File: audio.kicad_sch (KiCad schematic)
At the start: 1 part, among them U7 PCM5122PW

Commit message: External I/O
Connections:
- net AUDIO_L_OUT: now reaches U7.6 (OUTL)
- net AUDIO_R_OUT: now reaches U7.7 (OUTR)
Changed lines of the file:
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@@
+		)
+	)
+	(hierarchical_label "AUDIO_L_OUT"
+		(shape output)
+		(at 165.1 82.55 0)
+		(effects
+			(font
+				(size 1.27 1.27)
+			)
+			(justify left)
+		)
+	)
+	(hierarchical_label "AUDIO_R_OUT"
+		(shape output)
+		(at 165.1 85.09 0)
+		(effects
+			(font
+				(size 1.27 1.27)
+			)
+			(justify left)
 		)
 	)

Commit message: Internal Connectors
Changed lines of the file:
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@@
 	(bus
 		(pts
-			(xy 121.92 80.01) (xy 116.84 80.01)
+			(xy 121.92 80.01) (xy 121.92 77.47)
 		)
 		(stroke
@@
 	(hierarchical_label "{I2S}"
 		(shape input)
-		(at 116.84 80.01 180)
+		(at 121.92 77.47 90)
 		(effects
 			(font
 				(size 1.27 1.27)
 			)
-			(justify right)
+			(justify left)
 		)
 	)

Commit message: Cleanup & Debug I/O
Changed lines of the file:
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@@
+		)
+	)
+	(hierarchical_label "AUD_RST_N"
+		(shape input)
+		(at 120.65 100.33 180)
+		(effects
+			(font
+				(size 1.27 1.27)
+			)
+			(justify right)
 		)
 	)

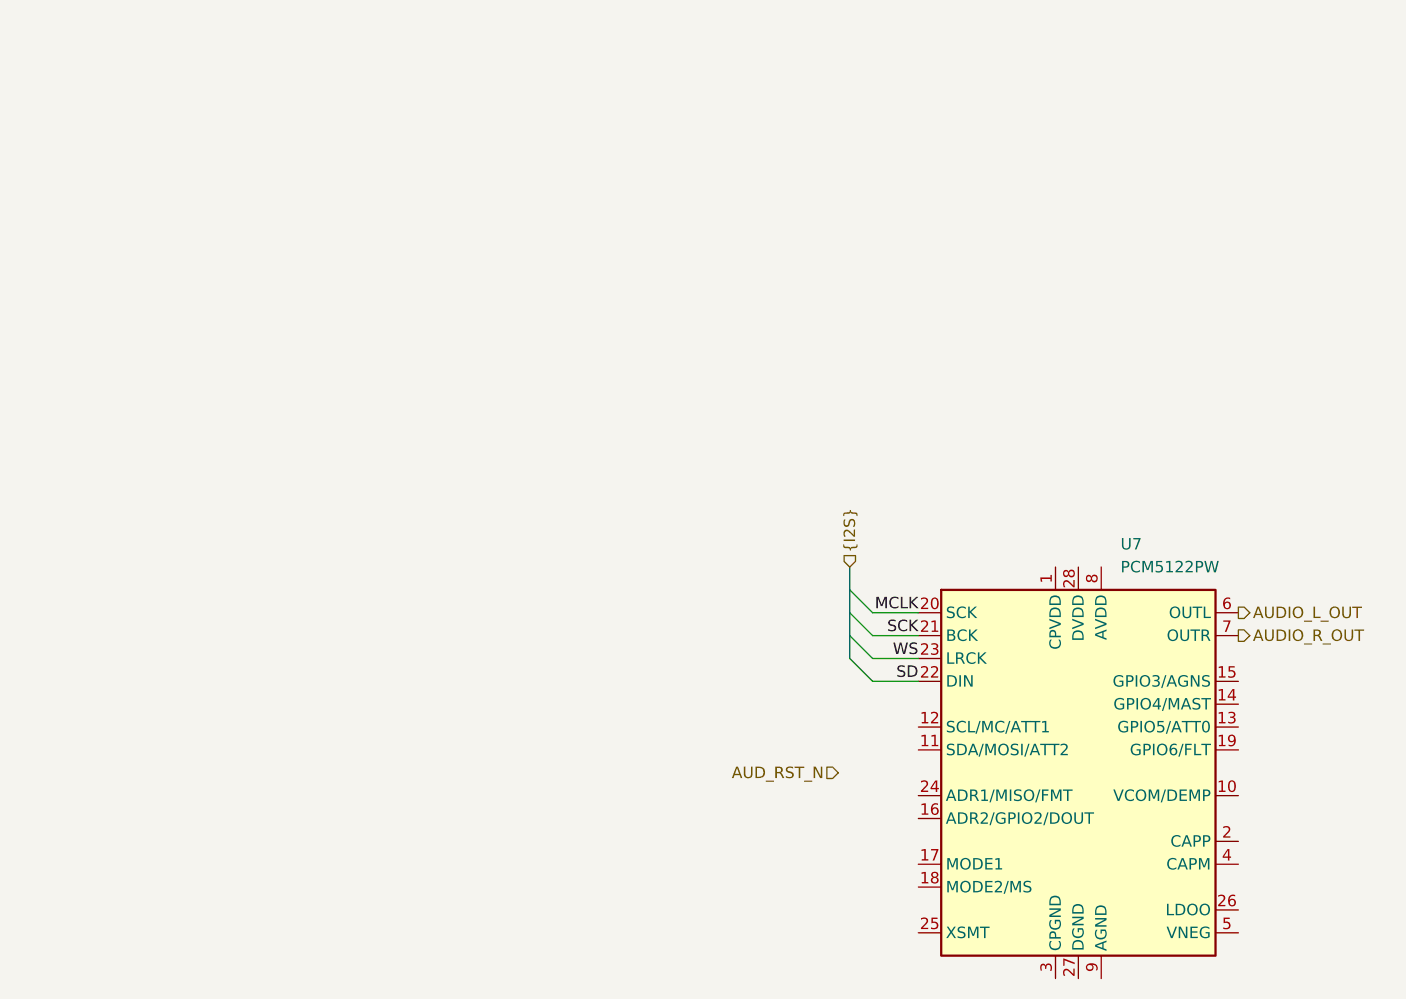
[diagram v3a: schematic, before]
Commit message: Audio Output, Analog isolation and TOSLINK
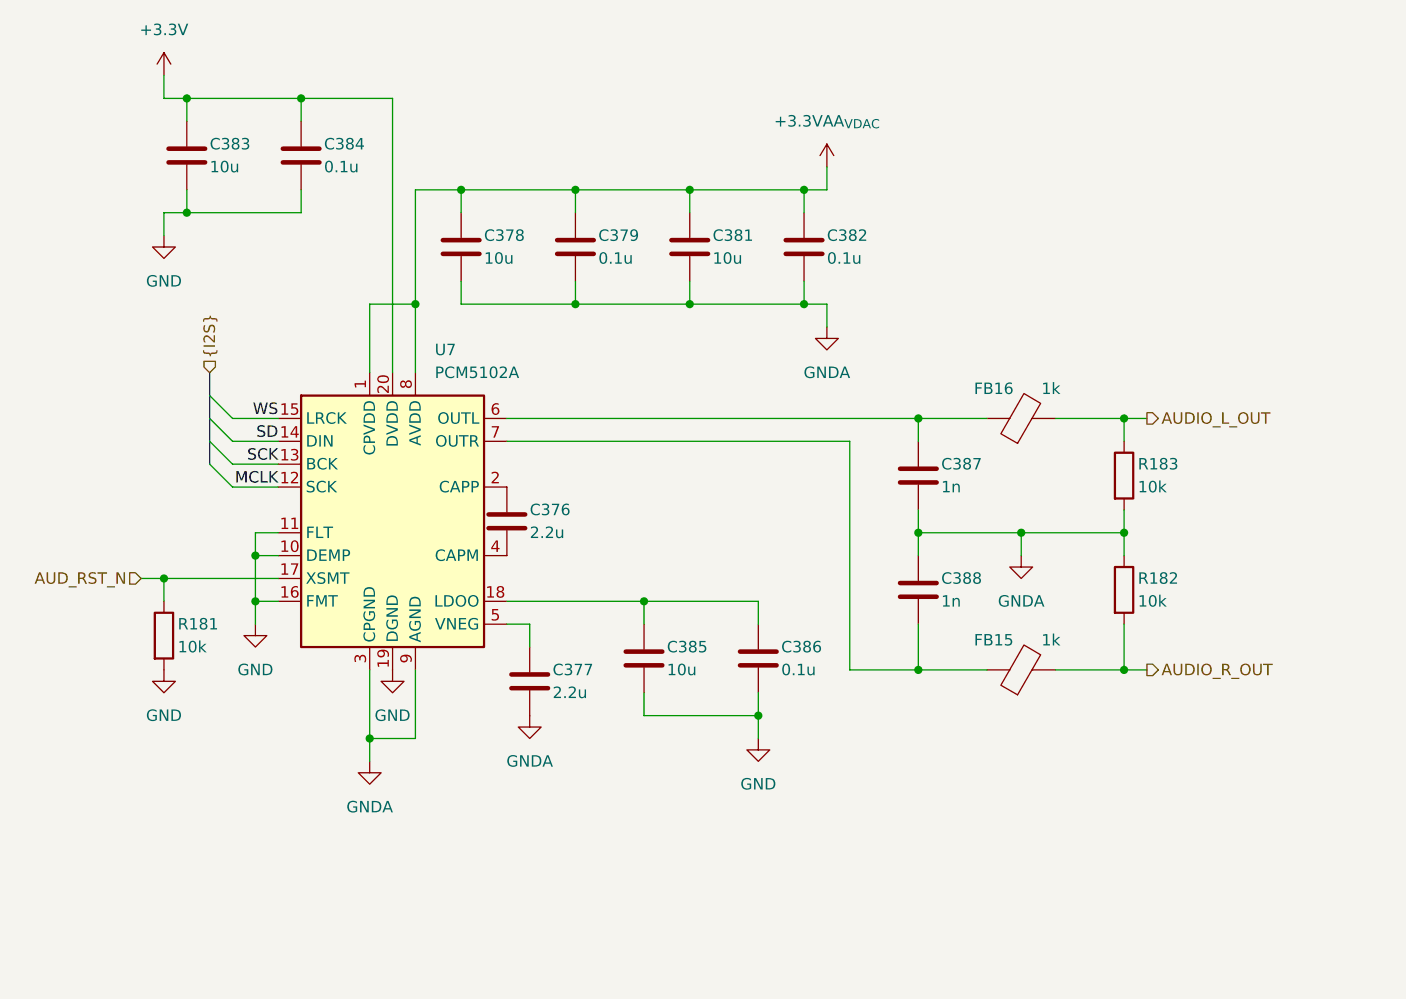
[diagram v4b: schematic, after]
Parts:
- removed U7: PCM5122PW, Package_SO:TSSOP-28_4.4x9.7mm_P0.65mm, symbol Audio:PCM5122PW
- added C376, C377: 2.2u, symbol Device:C
- added C378, C381, C383, C385: 10u, symbol Device:C
- added C379, C382, C384, C386: 0.1u, symbol Device:C
- added C387, C388: 1n, symbol Device:C
- added FB15, FB16: 1k, symbol Device:FerriteBead
- added R181, R182, R183: 10k, symbol Device:R
- added U7: PCM5102A, Package_SO:TSSOP-20_4.4x6.5mm_P0.65mm, symbol Audio:PCM5102A
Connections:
- net AUDIO_L_OUT: now also FB16.2, R183.1
- net AUDIO_R_OUT: now also FB15.2, R182.2
- net AUD_RST_N: now also R181.1, U7.17 (XSMT)
- net MCLK: now also U7.12 (SCK)
- net SCK: now also U7.13 (BCK)
- net SD: now also U7.14 (DIN)
- net WS: now also U7.15 (LRCK)
- new net: C377.1, U7.5 (VNEG)
- new net: C376.1, U7.2 (CAPP)
- new net: C376.2, U7.4 (CAPM)
- new net: C385.1, C386.1, U7.18 (LDOO)
- new net: C387.1, FB16.1, U7.6 (OUTL)
- new net: C388.2, FB15.1, U7.7 (OUTR)
- new net +3.3V: C383.1, C384.1, U7.20 (DVDD)
- new net +3.3VAA_{VDAC}: C378.1, C379.1, C381.1, C382.1, U7.1 (CPVDD), U7.8 (AVDD)
- new net GND: C383.2, C384.2, C385.2, C386.2, R181.2, U7.10 (DEMP), U7.11 (FLT), U7.16 (FMT), U7.19 (DGND)
- new net GNDA: C377.2, C378.2, C379.2, C381.2, C382.2, C387.2, C388.1, R182.1, R183.2, U7.3 (CPGND), U7.9 (AGND)

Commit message: Multipurpose and standby power rails, Reannotated schematic
Added V_1P2, V_1P8, V_5P0DUAL, V_EFUSE, V_GPUPCIE, V_3P3STBY and V_1P2STBY
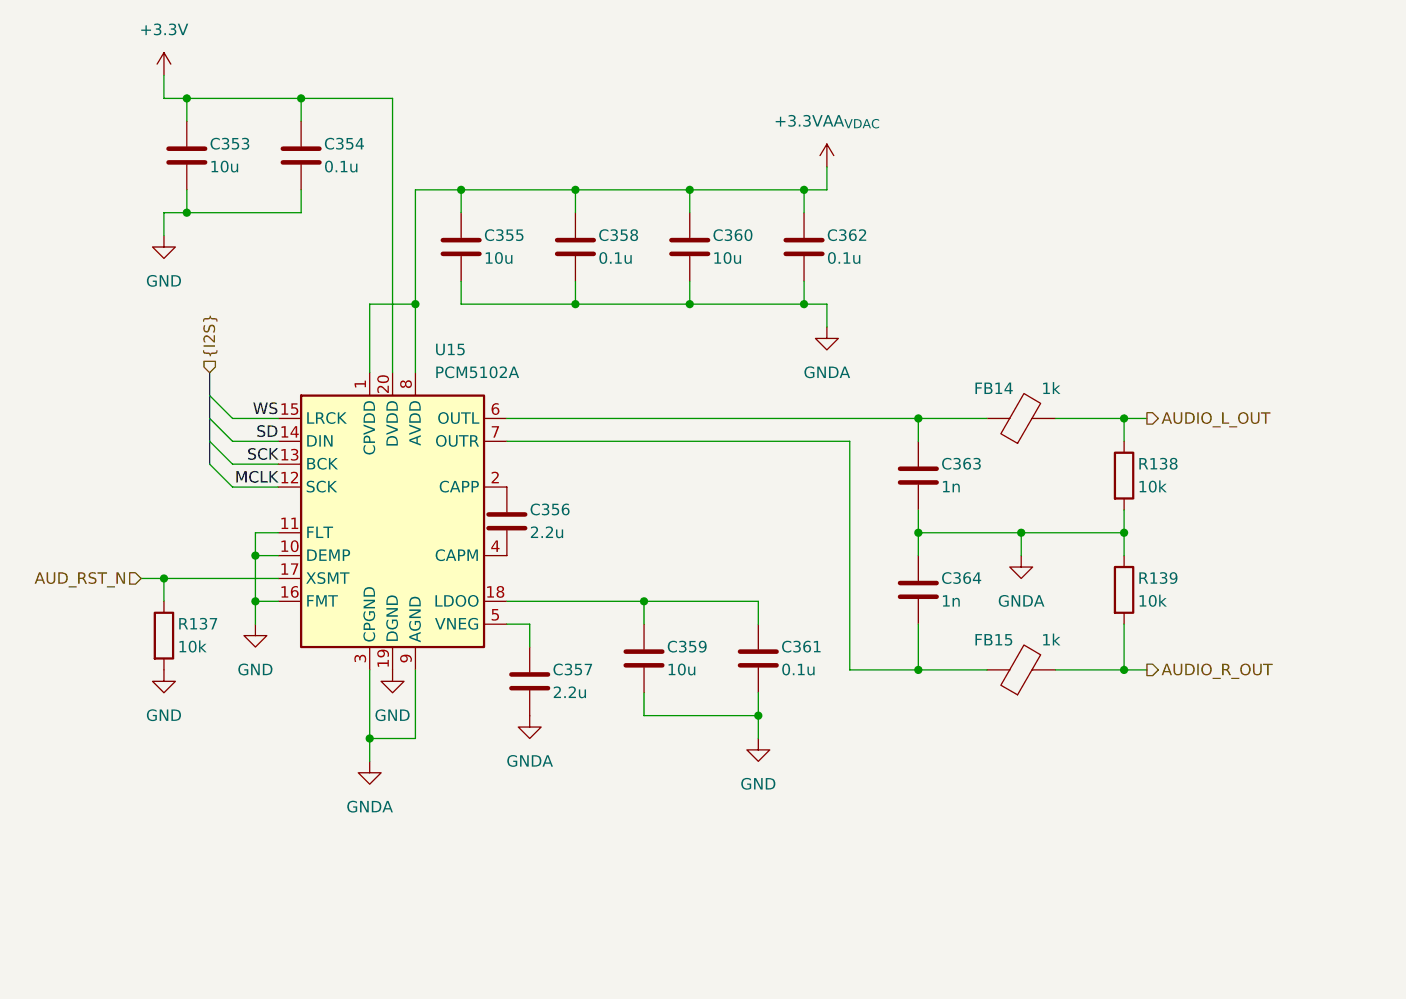
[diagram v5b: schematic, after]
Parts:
- renumbered C383 to C353, C384 to C354, C378 to C355, C376 to C356, C377 to C357, C379 to C358, C385 to C359, C381 to C360, C386 to C361, C382 to C362, C387 to C363, C388 to C364, FB16 to FB14, R181 to R137, R183 to R138, R182 to R139, U7 to U15
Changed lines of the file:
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@@
 		(on_board yes)
 		(dnp no)
-		(property "Reference" "C384"
+		(property "Reference" "C354"
 			(at 63.5 30.48 0)
 			(effects
@@
 			(project "Mantaray"
 				(path "/16640ecb-e4a4-4594-871b-70047bfba6e0/06303de4-2744-44da-b431-31b4ad95c62e"
-					(reference "C384")
+					(reference "C354")
 					(unit 1)
 				)
@@
 		(on_board yes)
 		(dnp no)
-		(property "Reference" "C377"
+		(property "Reference" "C357"
 			(at 88.9 88.9 0)
 			(effects
@@
 			(project "Mantaray"
 				(path "/16640ecb-e4a4-4594-871b-70047bfba6e0/06303de4-2744-44da-b431-31b4ad95c62e"
-					(reference "C377")
+					(reference "C357")
 					(unit 1)
 				)
@@
 		(dnp no)
 		(fields_autoplaced yes)
-		(property "Reference" "#PWR0367"
+		(property "Reference" "#PWR0257"
 			(at 119.38 36.83 0)
 			(effects
@@
 			(project "Mantaray"
 				(path "/16640ecb-e4a4-4594-871b-70047bfba6e0/06303de4-2744-44da-b431-31b4ad95c62e"
-					(reference "#PWR0367")
+					(reference "#PWR0257")
 					(unit 1)
 				)
@@
 		(dnp no)
 		(fields_autoplaced yes)
-		(property "Reference" "#PWR0372"
+		(property "Reference" "#PWR0256"
 			(at 111.76 102.87 0)
 			(effects
@@
 			(project "Mantaray"
 				(path "/16640ecb-e4a4-4594-871b-70047bfba6e0/06303de4-2744-44da-b431-31b4ad95c62e"
-					(reference "#PWR0372")
+					(reference "#PWR0256")
 					(unit 1)
 				)
@@
 		(on_board yes)
 		(dnp no)
-		(property "Reference" "C376"
+		(property "Reference" "C356"
 			(at 86.36 71.12 0)
 			(effects
@@
 			(project "Mantaray"
 				(path "/16640ecb-e4a4-4594-871b-70047bfba6e0/06303de4-2744-44da-b431-31b4ad95c62e"
-					(reference "C376")
+					(reference "C356")
 					(unit 1)
 				)
@@
 		(dnp no)
 		(fields_autoplaced yes)
-		(property "Reference" "#PWR0370"
+		(property "Reference" "#PWR0249"
 			(at 45.72 26.67 0)
 			(effects
@@
 			(project "Mantaray"
 				(path "/16640ecb-e4a4-4594-871b-70047bfba6e0/06303de4-2744-44da-b431-31b4ad95c62e"
-					(reference "#PWR0370")
+					(reference "#PWR0249")
 					(unit 1)
 				)
@@
 		(on_board yes)
 		(dnp no)
-		(property "Reference" "C385"
+		(property "Reference" "C359"
 			(at 101.6 86.36 0)
 			(effects
@@
 			(project "Mantaray"
 				(path "/16640ecb-e4a4-4594-871b-70047bfba6e0/06303de4-2744-44da-b431-31b4ad95c62e"
-					(reference "C385")
+					(reference "C359")
 					(unit 1)
 				)
@@
 		(on_board yes)
 		(dnp no)
-		(property "Reference" "R182"
+		(property "Reference" "R139"
 			(at 153.924 78.74 0)
 			(effects
@@
 			(project "Mantaray"
 				(path "/16640ecb-e4a4-4594-871b-70047bfba6e0/06303de4-2744-44da-b431-31b4ad95c62e"
-					(reference "R182")
+					(reference "R139")
 					(unit 1)
 				)
@@
 		(on_board yes)
 		(dnp no)
-		(property "Reference" "C387"
+		(property "Reference" "C363"
 			(at 132.08 66.04 0)
 			(effects
@@
 			(project "Mantaray"
 				(path "/16640ecb-e4a4-4594-871b-70047bfba6e0/06303de4-2744-44da-b431-31b4ad95c62e"
-					(reference "C387")
+					(reference "C363")
 					(unit 1)
 				)
@@
 		(on_board yes)
 		(dnp no)
-		(property "Reference" "C378"
+		(property "Reference" "C355"
 			(at 81.28 40.64 0)
 			(effects
@@
 			(project "Mantaray"
 				(path "/16640ecb-e4a4-4594-871b-70047bfba6e0/06303de4-2744-44da-b431-31b4ad95c62e"
-					(reference "C378")
+					(reference "C355")
 					(unit 1)
 				)
@@
 		(dnp no)
 		(fields_autoplaced yes)
-		(property "Reference" "#PWR0258"
+		(property "Reference" "#PWR0251"
 			(at 45.72 95.25 0)
 			(effects
@@
 			(project ""
 				(path "/16640ecb-e4a4-4594-871b-70047bfba6e0/06303de4-2744-44da-b431-31b4ad95c62e"
-					(reference "#PWR0258")
+					(reference "#PWR0251")
 					(unit 1)
 				)
@@
 		(dnp no)
 		(fields_autoplaced yes)
-		(property "Reference" "#PWR0371"
+		(property "Reference" "#PWR0254"
 			(at 71.12 95.25 0)
 			(effects
@@
 			(project ""
 				(path "/16640ecb-e4a4-4594-871b-70047bfba6e0/06303de4-2744-44da-b431-31b4ad95c62e"
-					(reference "#PWR0371")
+					(reference "#PWR0254")
 					(unit 1)
 				)
@@
 		(dnp no)
 		(fields_autoplaced yes)
-		(property "Reference" "U7"
+		(property "Reference" "U15"
 			(at 75.8033 53.34 0)
 			(effects
@@
 			(project ""
 				(path "/16640ecb-e4a4-4594-871b-70047bfba6e0/06303de4-2744-44da-b431-31b4ad95c62e"
-					(reference "U7")
+					(reference "U15")
 					(unit 1)
 				)
@@
 		(on_board yes)
 		(dnp no)
-		(property "Reference" "R181"
+		(property "Reference" "R137"
 			(at 47.244 83.82 0)
 			(effects
@@
 			(project "Mantaray"
 				(path "/16640ecb-e4a4-4594-871b-70047bfba6e0/06303de4-2744-44da-b431-31b4ad95c62e"
-					(reference "R181")
+					(reference "R137")
 					(unit 1)
 				)
@@
 		(on_board yes)
 		(dnp no)
-		(property "Reference" "C381"
+		(property "Reference" "C360"
 			(at 106.68 40.64 0)
 			(effects
@@
 			(project "Mantaray"
 				(path "/16640ecb-e4a4-4594-871b-70047bfba6e0/06303de4-2744-44da-b431-31b4ad95c62e"
-					(reference "C381")
+					(reference "C360")
 					(unit 1)
 				)
@@
 		(dnp no)
 		(fields_autoplaced yes)
-		(property "Reference" "#PWR0368"
+		(property "Reference" "#PWR0258"
 			(at 119.38 57.15 0)
 			(effects
@@
 			(project "Mantaray"
 				(path "/16640ecb-e4a4-4594-871b-70047bfba6e0/06303de4-2744-44da-b431-31b4ad95c62e"
-					(reference "#PWR0368")
+					(reference "#PWR0258")
 					(unit 1)
 				)
@@
 		(on_board yes)
 		(dnp no)
-		(property "Reference" "FB16"
+		(property "Reference" "FB14"
 			(at 137.922 57.658 90)
 			(effects
@@
 			(project "Mantaray"
 				(path "/16640ecb-e4a4-4594-871b-70047bfba6e0/06303de4-2744-44da-b431-31b4ad95c62e"
-					(reference "FB16")
+					(reference "FB14")
 					(unit 1)
 				)
@@
 		(on_board yes)
 		(dnp no)
-		(property "Reference" "C379"
+		(property "Reference" "C358"
 			(at 93.98 40.64 0)
 			(effects
@@
 			(project "Mantaray"
 				(path "/16640ecb-e4a4-4594-871b-70047bfba6e0/06303de4-2744-44da-b431-31b4ad95c62e"
-					(reference "C379")
+					(reference "C358")
 					(unit 1)
 				)
@@
 		(dnp no)
 		(fields_autoplaced yes)
-		(property "Reference" "#PWR0373"
+		(property "Reference" "#PWR0259"
 			(at 140.97 82.55 0)
 			(effects
@@
 			(project "Mantaray"
 				(path "/16640ecb-e4a4-4594-871b-70047bfba6e0/06303de4-2744-44da-b431-31b4ad95c62e"
-					(reference "#PWR0373")
+					(reference "#PWR0259")
 					(unit 1)
 				)
@@
 		(dnp no)
 		(fields_autoplaced yes)
-		(property "Reference" "#PWR0215"
+		(property "Reference" "#PWR0255"
 			(at 86.36 100.33 0)
 			(effects
@@
 			(project "Mantaray"
 				(path "/16640ecb-e4a4-4594-871b-70047bfba6e0/06303de4-2744-44da-b431-31b4ad95c62e"
-					(reference "#PWR0215")
+					(reference "#PWR0255")
 					(unit 1)
 				)
@@
 		(on_board yes)
 		(dnp no)
-		(property "Reference" "C386"
+		(property "Reference" "C361"
 			(at 114.3 86.36 0)
 			(effects
@@
 			(project "Mantaray"
 				(path "/16640ecb-e4a4-4594-871b-70047bfba6e0/06303de4-2744-44da-b431-31b4ad95c62e"
-					(reference "C386")
+					(reference "C361")
 					(unit 1)
 				)
@@
 		(on_board yes)
 		(dnp no)
-		(property "Reference" "R183"
+		(property "Reference" "R138"
 			(at 153.924 66.04 0)
 			(effects
@@
 			(project "Mantaray"
 				(path "/16640ecb-e4a4-4594-871b-70047bfba6e0/06303de4-2744-44da-b431-31b4ad95c62e"
-					(reference "R183")
+					(reference "R138")
 					(unit 1)
 				)
@@
 		(on_board yes)
 		(dnp no)
-		(property "Reference" "C388"
+		(property "Reference" "C364"
 			(at 132.08 78.74 0)
 			(effects
@@
 			(project "Mantaray"
 				(path "/16640ecb-e4a4-4594-871b-70047bfba6e0/06303de4-2744-44da-b431-31b4ad95c62e"
-					(reference "C388")
+					(reference "C364")
 					(unit 1)
 				)
@@
 		(dnp no)
 		(fields_autoplaced yes)
-		(property "Reference" "#PWR0369"
+		(property "Reference" "#PWR0250"
 			(at 45.72 46.99 0)
 			(effects
@@
 			(project ""
 				(path "/16640ecb-e4a4-4594-871b-70047bfba6e0/06303de4-2744-44da-b431-31b4ad95c62e"
-					(reference "#PWR0369")
+					(reference "#PWR0250")
 					(unit 1)
 				)
@@
 		(dnp no)
 		(fields_autoplaced yes)
-		(property "Reference" "#PWR0162"
+		(property "Reference" "#PWR0253"
 			(at 68.58 105.41 0)
 			(effects
@@
 			(project ""
 				(path "/16640ecb-e4a4-4594-871b-70047bfba6e0/06303de4-2744-44da-b431-31b4ad95c62e"
-					(reference "#PWR0162")
+					(reference "#PWR0253")
 					(unit 1)
 				)
@@
 		(on_board yes)
 		(dnp no)
-		(property "Reference" "C382"
+		(property "Reference" "C362"
 			(at 119.38 40.64 0)
 			(effects
@@
 			(project "Mantaray"
 				(path "/16640ecb-e4a4-4594-871b-70047bfba6e0/06303de4-2744-44da-b431-31b4ad95c62e"
-					(reference "C382")
+					(reference "C362")
 					(unit 1)
 				)
@@
 		(dnp no)
 		(fields_autoplaced yes)
-		(property "Reference" "#PWR0302"
+		(property "Reference" "#PWR0252"
 			(at 55.88 90.17 0)
 			(effects
@@
 			(project "Mantaray"
 				(path "/16640ecb-e4a4-4594-871b-70047bfba6e0/06303de4-2744-44da-b431-31b4ad95c62e"
-					(reference "#PWR0302")
+					(reference "#PWR0252")
 					(unit 1)
 				)
@@
 		(on_board yes)
 		(dnp no)
-		(property "Reference" "C383"
+		(property "Reference" "C353"
 			(at 50.8 30.48 0)
 			(effects
@@
 			(project "Mantaray"
 				(path "/16640ecb-e4a4-4594-871b-70047bfba6e0/06303de4-2744-44da-b431-31b4ad95c62e"
-					(reference "C383")
-					(unit 1)
-				)
+					(reference "C353")
+					(unit 1)
+				)
